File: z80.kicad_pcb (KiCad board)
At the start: 2 copper layers, 215.9 x 132.1 mm, 106 parts, among them CON1 BARREL_JACK, CON1002 BARREL_JACK, SW1 RESET, SW2 STEP, U1 Z80CPU, U1001 TL2575-5, U1002 LM7805CT, U2 74HC04, U3 74AC541, U4 74LS138, U5 74HC245, U6 74LS148, Y1 7.3728MHz

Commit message: PCB layout complete, passes DRC, more tuning required
One thing not enough buffers for all address lines (missed A5), so
swapped out the CLK. Not sure if that was a good idea, but didn't want
to add another chip for a single buffer. :(
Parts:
- removed C1003: 100u, Capacitors_SMD:C_0201
- removed C1004: 10u, Capacitors_SMD:C_0201
- removed C12: 100u, Capacitors_SMD:c_elec_6.3x4.5
- removed C13: 330u, Capacitors_SMD:c_elec_6.3x4.5
- removed CON1, CON1002: BARREL_JACK, Connect:BARREL_JACK
- removed D10, D11, D12, D9: 11DQ06, Diodes_SMD:DO-214AB_Handsoldering
- removed D1003, D1004: 11DQ06, Diodes_SMD:DO-214AB
- removed L1: 330uH / 1A, Inductors_NEOSID:Neosid_Inductor_SM-PIC1004H
- removed U1001: TL2575-5, TO_SOT_Packages_SMD:TO-263-5Lead
- removed U1002: LM7805CT, Power_Integrations:TO-220
- moved R21 318.9 mm to (51.9, 36.8), turned to 180 degrees
- moved D1 315.4 mm to (57.0, 36.8)
- moved R1 299.2 mm to (56.4, 103.5), turned to 180 degrees
- moved D6 223.1 mm to (143.3, 102.4)
- moved D7 221.1 mm to (143.3, 104.9)
- moved D5 220.6 mm to (143.3, 99.8)
- moved D4 218.5 mm to (143.3, 107.4)
- moved R17 216.0 mm to (138.2, 107.4), turned to 180 degrees
- moved R6 212.1 mm to (74.8, 97.8), turned to 270 degrees
- moved R9 210.5 mm to (74.8, 113.0), turned to 270 degrees
- moved R20 208.7 mm to (138.2, 104.9), turned to 180 degrees
- moved R18 199.1 mm to (138.2, 99.8), turned to 180 degrees
- moved R19 191.1 mm to (138.2, 102.4), turned to 180 degrees
- moved C10 128.7 mm to (133.6, 120.9)
- moved C9 122.2 mm to (121.2, 113.8), turned to 90 degrees
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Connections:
- C11 pad 1: Net-(C11-Pad1) -> VCC
- PIA1 pad 1: /IO/A5-B -> VCC
- PIA1 pad 10: /~INT -> /IO/A1-B
- PIA1 pad 11: /IO/~CLK-B -> /IO/A0-B
- PIA1 pad 12: /~RESET -> /IO/~RD-B
- PIA1 pad 13: VCC -> /IO/~WR-B
- PIA1 pad 14: GND -> /IO/~IOSEL1
- PIA1 pad 2: /IO/A4-B -> GND
- PIA1 pad 3: /IO/A3-B -> /~RESET
- PIA1 pad 4: /IO/A2-B -> /~CLK
- PIA1 pad 5: /IO/A1-B -> /~INT
- PIA1 pad 6: /IO/A0-B -> /IO/A5-B
- PIA1 pad 7: /IO/~IOSEL1 -> /IO/A4-B
- PIA1 pad 8: /IO/~RD-B -> /IO/A3-B
- PIA1 pad 9: /IO/~WR-B -> /IO/A2-B
- PIB1 pad 1: /IO/A5-B -> VCC
- PIB1 pad 10: /~INT -> /IO/A1-B
- PIB1 pad 11: /IO/~CLK-B -> /IO/A0-B
- PIB1 pad 12: /~RESET -> /IO/~RD-B
- PIB1 pad 13: VCC -> /IO/~WR-B
- PIB1 pad 14: GND -> /IO/~IOSEL2
- PIB1 pad 2: /IO/A4-B -> GND
- PIB1 pad 3: /IO/A3-B -> /~RESET
- PIB1 pad 4: /IO/A2-B -> /~CLK
- PIB1 pad 5: /IO/A1-B -> /~INT
- PIB1 pad 6: /IO/A0-B -> /IO/A5-B
- PIB1 pad 7: /IO/~IOSEL2 -> /IO/A4-B
- PIB1 pad 8: /IO/~RD-B -> /IO/A3-B
- PIB1 pad 9: /IO/~WR-B -> /IO/A2-B
- PIC1 pad 1: /IO/A5-B -> VCC
- PIC1 pad 10: /~INT -> /IO/A1-B
- PIC1 pad 11: /IO/~CLK-B -> /IO/A0-B
- PIC1 pad 12: /~RESET -> /IO/~RD-B
- PIC1 pad 13: VCC -> /IO/~WR-B
- PIC1 pad 14: GND -> /IO/~IOSEL3
- PIC1 pad 2: /IO/A4-B -> GND
- PIC1 pad 3: /IO/A3-B -> /~RESET
- PIC1 pad 4: /IO/A2-B -> /~CLK
- PIC1 pad 5: /IO/A1-B -> /~INT
- PIC1 pad 6: /IO/A0-B -> /IO/A5-B
- PIC1 pad 7: /IO/~IOSEL3 -> /IO/A4-B
- PIC1 pad 8: /IO/~RD-B -> /IO/A3-B
- PIC1 pad 9: /IO/~WR-B -> /IO/A2-B
- PID1 pad 1: /IO/A5-B -> VCC
- PID1 pad 10: /~INT -> /IO/A1-B
- PID1 pad 11: /IO/~CLK-B -> /IO/A0-B
- PID1 pad 12: /~RESET -> /IO/~RD-B
- PID1 pad 13: VCC -> /IO/~WR-B
- PID1 pad 14: GND -> /IO/~IOSEL4
- PID1 pad 2: /IO/A4-B -> GND
- PID1 pad 3: /IO/A3-B -> /~RESET
- PID1 pad 4: /IO/A2-B -> /~CLK
- PID1 pad 5: /IO/A1-B -> /~INT
- PID1 pad 6: /IO/A0-B -> /IO/A5-B
- PID1 pad 7: /IO/~IOSEL4 -> /IO/A4-B
- PID1 pad 8: /IO/~RD-B -> /IO/A3-B
- PID1 pad 9: /IO/~WR-B -> /IO/A2-B
- PIE1 pad 1: /IO/A5-B -> VCC
- PIE1 pad 10: /~INT -> /IO/A1-B
- PIE1 pad 11: /IO/~CLK-B -> /IO/A0-B
- PIE1 pad 12: /~RESET -> /IO/~RD-B
- PIE1 pad 13: VCC -> /IO/~WR-B
- PIE1 pad 14: GND -> /IO/~IOSEL5
- PIE1 pad 2: /IO/A4-B -> GND
- PIE1 pad 3: /IO/A3-B -> /~RESET
- PIE1 pad 4: /IO/A2-B -> /~CLK
- PIE1 pad 5: /IO/A1-B -> /~INT
- PIE1 pad 6: /IO/A0-B -> /IO/A5-B
- PIE1 pad 7: /IO/~IOSEL5 -> /IO/A4-B
- PIE1 pad 8: /IO/~RD-B -> /IO/A3-B
- PIE1 pad 9: /IO/~WR-B -> /IO/A2-B
- PIF1 pad 1: /IO/A5-B -> VCC
- PIF1 pad 10: /~INT -> /IO/A1-B
- PIF1 pad 11: /IO/~CLK-B -> /IO/A0-B
- PIF1 pad 12: /~RESET -> /IO/~RD-B
- PIF1 pad 13: VCC -> /IO/~WR-B
- PIF1 pad 14: GND -> /IO/~IOSEL6
- PIF1 pad 2: /IO/A4-B -> GND
- PIF1 pad 3: /IO/A3-B -> /~RESET
- PIF1 pad 4: /IO/A2-B -> /~CLK
- PIF1 pad 5: /IO/A1-B -> /~INT
- PIF1 pad 6: /IO/A0-B -> /IO/A5-B
- PIF1 pad 7: /IO/~IOSEL6 -> /IO/A4-B
- PIF1 pad 8: /IO/~RD-B -> /IO/A3-B
- PIF1 pad 9: /IO/~WR-B -> /IO/A2-B
- PIG1 pad 1: /IO/A5-B -> VCC
- PIG1 pad 10: /~INT -> /IO/A1-B
- PIG1 pad 11: /IO/~CLK-B -> /IO/A0-B
- PIG1 pad 12: /~RESET -> /IO/~RD-B
- PIG1 pad 13: VCC -> /IO/~WR-B
- PIG1 pad 14: GND -> /IO/~IOSEL7
- PIG1 pad 2: /IO/A4-B -> GND
- PIG1 pad 3: /IO/A3-B -> /~RESET
- PIG1 pad 4: /IO/A2-B -> /~CLK
- PIG1 pad 5: /IO/A1-B -> /~INT
- PIG1 pad 6: /IO/A0-B -> /IO/A5-B
- PIG1 pad 7: /IO/~IOSEL7 -> /IO/A4-B
- PIG1 pad 8: /IO/~RD-B -> /IO/A3-B
- PIG1 pad 9: /IO/~WR-B -> /IO/A2-B
- PIH1 pad 1: /IO/A5-B -> VCC
- PIH1 pad 10: /~INT -> /IO/A1-B
- PIH1 pad 11: /IO/~CLK-B -> /IO/A0-B
- PIH1 pad 12: /~RESET -> /IO/~RD-B
- PIH1 pad 13: VCC -> /IO/~WR-B
- PIH1 pad 14: GND -> /IO/~IOSEL8
- PIH1 pad 2: /IO/A4-B -> GND
- PIH1 pad 3: /IO/A3-B -> /~RESET
- PIH1 pad 4: /IO/A2-B -> /~CLK
- PIH1 pad 5: /IO/A1-B -> /~INT
- PIH1 pad 6: /IO/A0-B -> /IO/A5-B
- PIH1 pad 7: /IO/~IOSEL8 -> /IO/A4-B
- PIH1 pad 8: /IO/~RD-B -> /IO/A3-B
- PIH1 pad 9: /IO/~WR-B -> /IO/A2-B
- U3 pad 11: /IO/~CLK-B -> /IO/~WR-B
- U3 pad 12: /IO/~WR-B -> /IO/~RD-B
- U3 pad 13: /IO/~RD-B -> /IO/A0-B
- U3 pad 14: /IO/A0-B -> /IO/A1-B
- U3 pad 15: /IO/A1-B -> /IO/A2-B
- U3 pad 16: /IO/A2-B -> /IO/A3-B
- U3 pad 17: /IO/A3-B -> /IO/A4-B
- U3 pad 18: /IO/A4-B -> /IO/A5-B
- U3 pad 2: /A4 -> /A5
- U3 pad 3: /A3 -> /A4
- U3 pad 4: /A2 -> /A3
- U3 pad 5: /A1 -> /A2
- U3 pad 6: /A0 -> /A1
- U3 pad 7: /~RD -> /A0
- U3 pad 8: /~WR -> /~RD
- U3 pad 9: /~CLK -> /~WR
- USB1 pad 1: Net-(C11-Pad1) -> VCC
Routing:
- net VCC: track 161.5 -> 559.4 mm, vias 2 -> 9
- net /~INT: track 72.4 -> 280.9 mm, vias 1 -> 2
- net /IO/~IOSEL8: track 0.00 -> 169.3 mm, vias 0 -> 1
- net /IO/D6-B: track 0.00 -> 163.5 mm, vias 0 -> 1
- net /IO/D4-B: track 0.00 -> 162.9 mm, vias 0 -> 1
- net /IO/D5-B: track 0.00 -> 162.8 mm, vias 0 -> 1
- net /IO/D3-B: track 0.00 -> 162.7 mm, vias 0 -> 1
- net /~RESET: track 194.5 -> 357.1 mm, vias 0 -> 2
- net /IO/D0-B: track 0.00 -> 162.3 mm
- net /IO/D2-B: track 0.00 -> 162.1 mm, vias 0 -> 1
- net GND: track 136.6 -> 281.2 mm, vias 5 -> 9
- net /IO/~IOSEL7: track 0.00 -> 137.1 mm
- net /IO/~IOSEL6: track 0.00 -> 125.2 mm
- net /~CLK: track 173.5 -> 296.6 mm
- net /IO/A0-B: track 0.00 -> 116.1 mm
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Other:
- board size 215.9 x 132.1 mm -> 215.9 x 123.2 mm
- net class power added: clearance 0.1524, trace_width 0.5, via_dia 0.6858, via_drill 0.3302

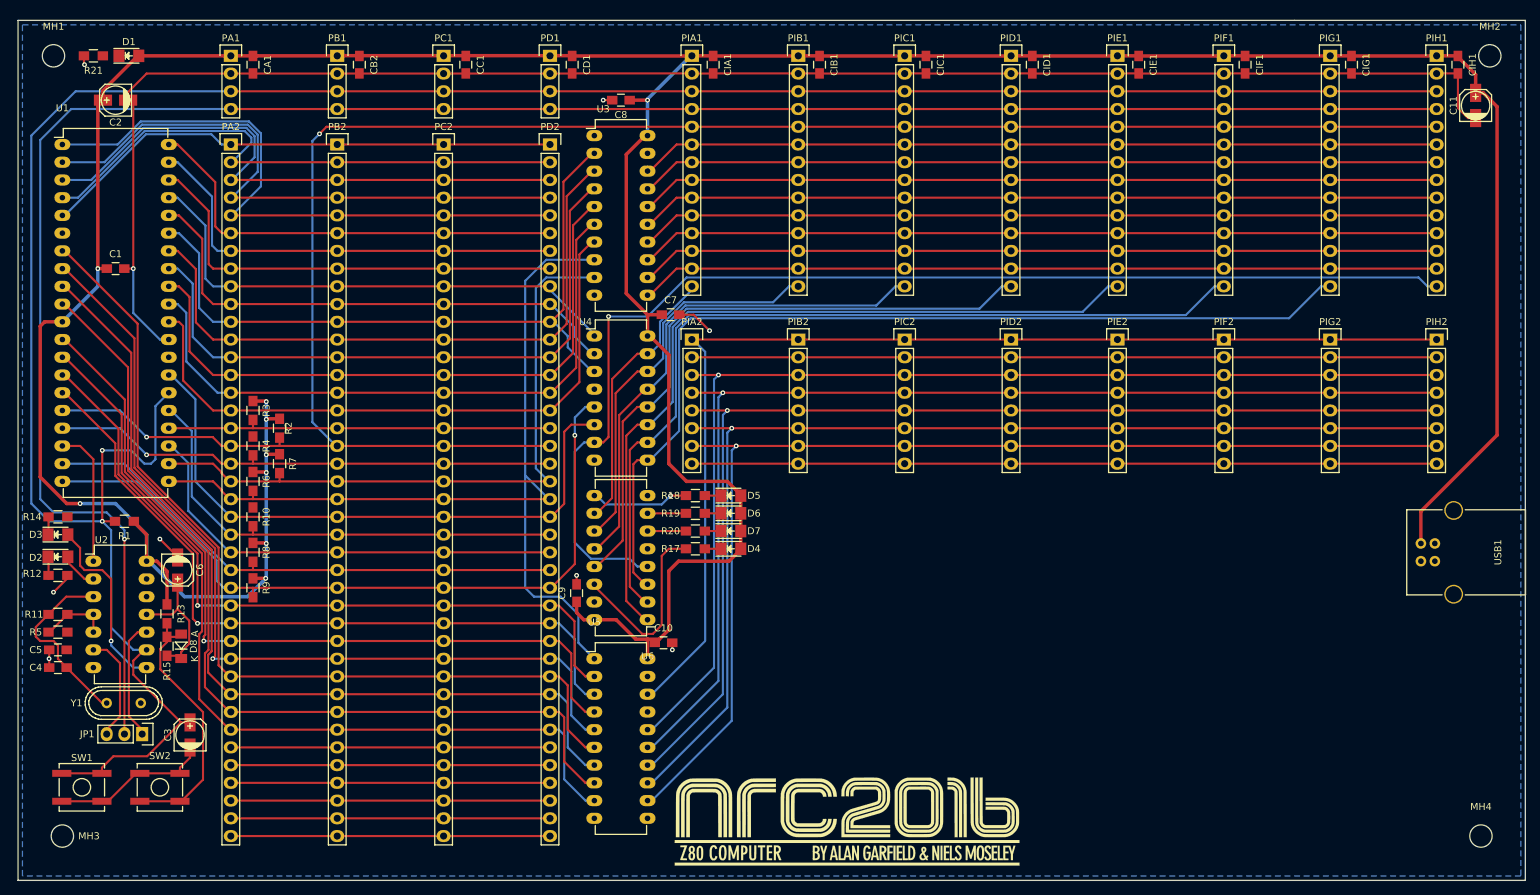
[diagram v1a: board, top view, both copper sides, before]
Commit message: Update with smaller board and through-hole parts.
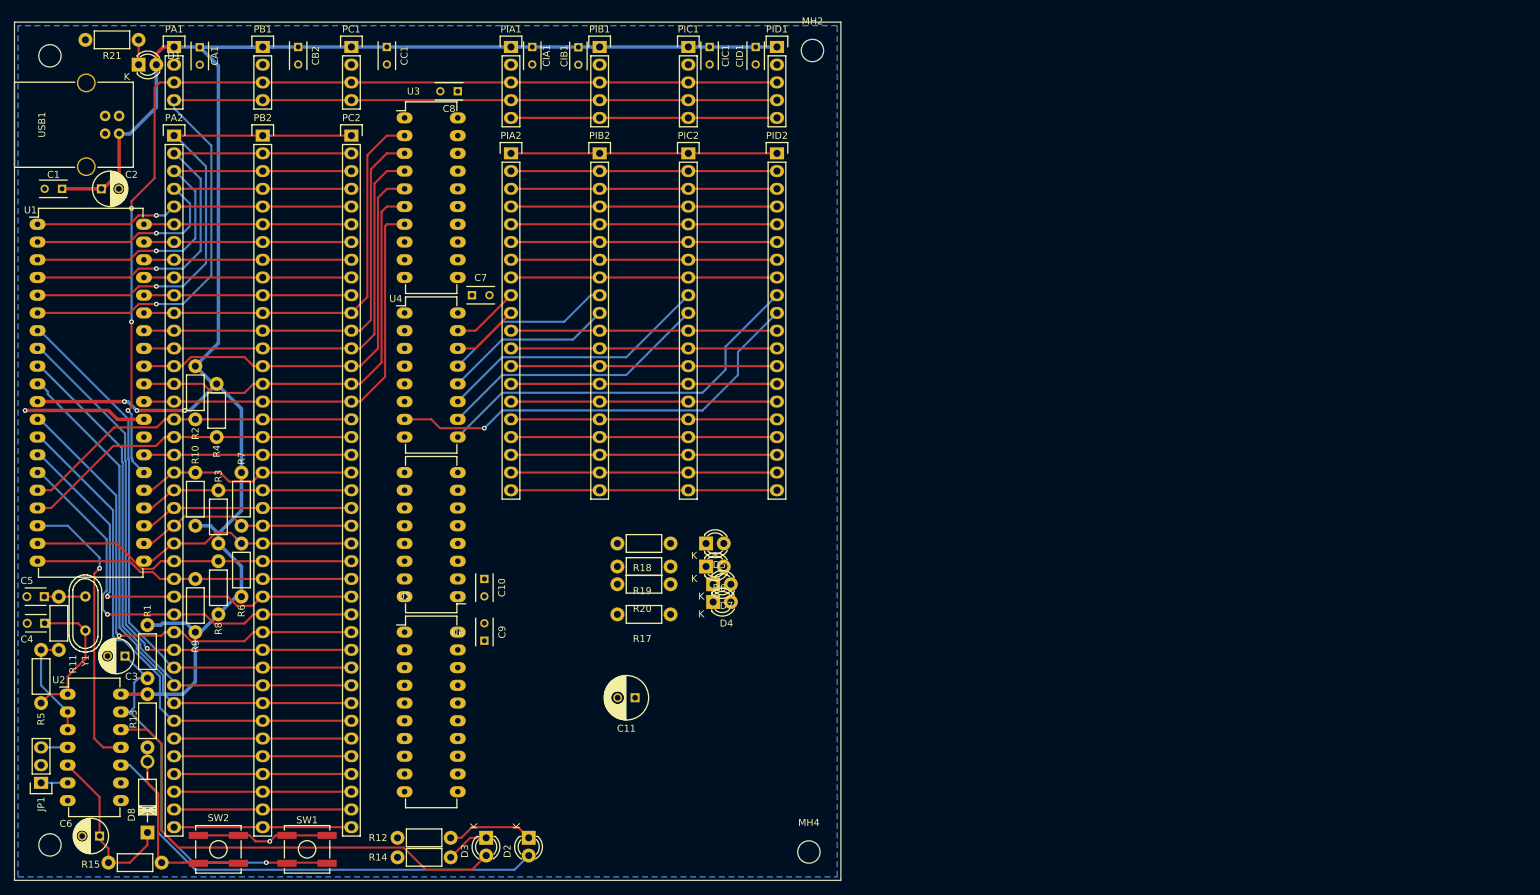
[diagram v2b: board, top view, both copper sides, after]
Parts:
- removed CD1, CIE1, CIF1, CIG1, CIH1: 100n, Capacitors_SMD:C_0805_HandSoldering
- removed G***: LOGO, ncr2016_logo:nrc2016_logo_1200
- removed PD1: CONN_01X04, Socket_Strips:Socket_Strip_Straight_1x04
- removed PD2: CONN_01X40, Socket_Strips:Socket_Strip_Straight_1x40
- removed PIE1, PIF1, PIG1, PIH1: CONN_01X14, Socket_Strips:Socket_Strip_Straight_1x14
- removed PIE2, PIF2, PIG2, PIH2: CONN_01X08, Socket_Strips:Socket_Strip_Straight_1x08
- C1, C10, C7, C8, C9, CA1, CB2, CC1, CIA1, CIB1, CIC1, CID1: footprint Capacitors_SMD:C_0805_HandSoldering -> Capacitors_ThroughHole:C_Rect_L4_W2.5_P2.5
- C11: footprint Capacitors_SMD:c_elec_4x5.3 -> Capacitors_ThroughHole:C_Radial_D6.3_L11.2_P2.5
- C2, C3: footprint Capacitors_SMD:c_elec_4x4.5 -> Capacitors_ThroughHole:C_Radial_D5_L6_P2.5
- C4, C5: footprint Capacitors_SMD:C_0805_HandSoldering -> Capacitors_ThroughHole:C_Disc_D3_P2.5
- C6: footprint Capacitors_SMD:c_elec_4x4.5 -> Capacitors_ThroughHole:C_Radial_D5_L11_P2.5
- D1, D2, D3, D4, D5, D6, D7: footprint LEDs:LED_1206 -> LEDs:LED-3MM
- D8: footprint Diodes_SMD:MiniMELF_Standard -> Diodes_ThroughHole:Diode_DO-41_SOD81_Horizontal_RM10
- PIA1, PIB1, PIC1, PID1: value CONN_01X14 -> CONN_01X05; footprint Socket_Strips:Socket_Strip_Straight_1x14 -> Socket_Strips:Socket_Strip_Straight_1x05
- PIA2, PIB2, PIC2, PID2: value CONN_01X08 -> CONN_01X20; footprint Socket_Strips:Socket_Strip_Straight_1x08 -> Socket_Strips:Socket_Strip_Straight_1x20
- R1, R10, R11, R12, R13, R14, R15, R17, R18, R19, R2, R20, R21, R3, R4, R5, R6, R7, R8, R9: footprint Resistors_SMD:R_0805_HandSoldering -> Resistors_ThroughHole:Resistor_Horizontal_RM7mm
- moved USB1 195.5 mm to (55.6, 48.0), turned to 180 degrees
- moved C11 147.3 mm to (129.5, 128.8), turned to 180 degrees
- moved MH2 97.0 mm to (154.9, 36.1)
- moved MH4 96.3 mm to (154.4, 150.9)
- moved D2 78.5 mm to (114.3, 148.8), turned to 270 degrees
- moved D3 75.2 mm to (108.2, 148.8), turned to 270 degrees
- moved R14 74.5 mm to (103.1, 151.6), turned to 180 degrees
- moved R12 67.7 mm to (103.1, 148.8), turned to 180 degrees
- moved PID2 42.8 mm to (149.9, 50.8)
- moved PIC2 40.9 mm to (137.2, 50.8)
- moved C6 39.7 mm to (52.8, 148.6), turned to 180 degrees
- moved CID1 39.7 mm to (146.8, 35.6)
- moved PIB2 39.0 mm to (124.5, 50.8)
- moved PIA2 37.2 mm to (111.8, 50.8)
- moved CIB1 34.6 mm to (121.4, 35.6)
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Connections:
- PA2 pad 17: /~WAIT -> /~INT
- PA2 pad 18: /~INT -> /~NMI
- PA2 pad 19: /~NMI -> /~M1
- PA2 pad 20: /~WR -> /~BUSRQ
- PA2 pad 21: /~RD -> /~WAIT
- PA2 pad 22: /~M1 -> /~BUSACK
- PA2 pad 23: /~BUSRQ -> /~WR
- PA2 pad 24: /~BUSACK -> /~RD
- PA2 pad 35: /Card Slots/S1 -> /S1
- PA2 pad 36: /Card Slots/S2 -> /S2
- PB2 pad 17: /~WAIT -> /~INT
- PB2 pad 18: /~INT -> /~NMI
- PB2 pad 19: /~NMI -> /~M1
- PB2 pad 20: /~WR -> /~BUSRQ
- PB2 pad 21: /~RD -> /~WAIT
- PB2 pad 22: /~M1 -> /~BUSACK
- PB2 pad 23: /~BUSRQ -> /~WR
- PB2 pad 24: /~BUSACK -> /~RD
- PB2 pad 35: /Card Slots/S1 -> /S1
- PB2 pad 36: /Card Slots/S2 -> /S2
- PC2 pad 17: /~WAIT -> /~INT
- PC2 pad 18: /~INT -> /~NMI
- PC2 pad 19: /~NMI -> /~M1
- PC2 pad 20: /~WR -> /~BUSRQ
- PC2 pad 21: /~RD -> /~WAIT
- PC2 pad 22: /~M1 -> /~BUSACK
- PC2 pad 23: /~BUSRQ -> /~WR
- PC2 pad 24: /~BUSACK -> /~RD
- PC2 pad 35: /Card Slots/S1 -> /S1
- PC2 pad 36: /Card Slots/S2 -> /S2
- PIA2 pad 1: /IO/D0-B -> /IO/A5-B
- PIA2 pad 2: /IO/D1-B -> /IO/A4-B
- PIA2 pad 3: /IO/D2-B -> /IO/A3-B
- PIA2 pad 4: /IO/D3-B -> /IO/A2-B
- PIA2 pad 5: /IO/D4-B -> /IO/A1-B
- PIA2 pad 6: /IO/D5-B -> /IO/A0-B
- PIA2 pad 7: /IO/D6-B -> /IO/~RD-B
- PIA2 pad 8: /IO/D7-B -> /IO/~WR-B
- PIB2 pad 1: /IO/D0-B -> /IO/A5-B
- PIB2 pad 2: /IO/D1-B -> /IO/A4-B
- PIB2 pad 3: /IO/D2-B -> /IO/A3-B
- PIB2 pad 4: /IO/D3-B -> /IO/A2-B
- PIB2 pad 5: /IO/D4-B -> /IO/A1-B
- PIB2 pad 6: /IO/D5-B -> /IO/A0-B
- PIB2 pad 7: /IO/D6-B -> /IO/~RD-B
- PIB2 pad 8: /IO/D7-B -> /IO/~WR-B
- PIC2 pad 1: /IO/D0-B -> /IO/A5-B
- PIC2 pad 2: /IO/D1-B -> /IO/A4-B
- PIC2 pad 3: /IO/D2-B -> /IO/A3-B
- PIC2 pad 4: /IO/D3-B -> /IO/A2-B
- PIC2 pad 5: /IO/D4-B -> /IO/A1-B
- PIC2 pad 6: /IO/D5-B -> /IO/A0-B
- PIC2 pad 7: /IO/D6-B -> /IO/~RD-B
- PIC2 pad 8: /IO/D7-B -> /IO/~WR-B
- PID2 pad 1: /IO/D0-B -> /IO/A5-B
- PID2 pad 2: /IO/D1-B -> /IO/A4-B
- PID2 pad 3: /IO/D2-B -> /IO/A3-B
- PID2 pad 4: /IO/D3-B -> /IO/A2-B
- PID2 pad 5: /IO/D4-B -> /IO/A1-B
- PID2 pad 6: /IO/D5-B -> /IO/A0-B
- PID2 pad 7: /IO/D6-B -> /IO/~RD-B
- PID2 pad 8: /IO/D7-B -> /IO/~WR-B
- U1 pad 28: Net-(U1-Pad28) -> (no net)
- U2 pad 1: /CPU/~HALT -> Net-(C4-Pad1)
- U2 pad 10: Net-(JP1-Pad1) -> Net-(D2-Pad2)
- U2 pad 11: Net-(C6-Pad1) -> /CPU/~HALT
- U2 pad 12: (no net) -> Net-(D3-Pad2)
- U2 pad 13: (no net) -> /~RESET
- U2 pad 2: Net-(D2-Pad2) -> Net-(R11-Pad1)
- U2 pad 3: Net-(C4-Pad1) -> Net-(R11-Pad1)
- U2 pad 4: Net-(R11-Pad1) -> Net-(JP1-Pad3)
- U2 pad 5: Net-(R11-Pad1) -> Net-(C6-Pad1)
- U2 pad 6: Net-(JP1-Pad3) -> Net-(JP1-Pad1)
- U2 pad 8: Net-(D3-Pad2) -> (no net)
- U2 pad 9: /~RESET -> (no net)
- U6 pad 15: Net-(U6-Pad15) -> (no net)
- USB1 pad 2: Net-(USB1-Pad2) -> (no net)
- USB1 pad 3: Net-(USB1-Pad3) -> (no net)
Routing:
- net VCC: track 559.4 -> 272.0 mm, vias 9 -> 3
- net GND: track 281.2 -> 36.8 mm, vias 9 -> 2
- net /~INT: track 280.9 -> 88.1 mm, vias 2 -> 0
- net /~CLK: track 296.6 -> 140.8 mm
- net /~RESET: track 357.1 -> 204.1 mm, vias 2 -> 4
- net /IO/D6-B: track 163.5 -> 38.1 mm, vias 1 -> 0
- net /IO/D4-B: track 162.9 -> 38.1 mm, vias 1 -> 0
- net /IO/D5-B: track 162.8 -> 38.1 mm, vias 1 -> 0
- net /IO/D3-B: track 162.7 -> 38.1 mm, vias 1 -> 0
- net /IO/D0-B: track 162.3 -> 38.1 mm
- net /IO/D2-B: track 162.1 -> 38.1 mm, vias 1 -> 0
- net /IO/~IOSEL8: track 169.3 -> 62.6 mm
- net /~RD: track 135.0 -> 32.8 mm
- net /IO/~IOSEL6: track 125.2 -> 39.3 mm
- net /IO/~IOSEL7: track 137.1 -> 56.1 mm
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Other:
- board size 215.9 x 123.2 mm -> 118.4 x 122.9 mm
